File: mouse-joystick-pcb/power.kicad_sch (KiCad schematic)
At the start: 10 parts, among them J301 2.1, U301 TPSM365R6V5RDNR

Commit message: Finish routing
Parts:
- C305: LCSC C2182652 -> C6119904; Manufacturer TDK Corporation -> HRE; Manufacturer Part Number C2012X5R1A476M125AC -> CGA0805X5R476M100MT; Vendor Digi-Key -> JLCPCB; Vendor Part Number 445-8239-1-ND -> C6119904
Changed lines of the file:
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@@
   (title_block
     (title "mouse-joystick-pcb")
-    (date "2024-10-15")
+    (date "2024-10-23")
     (rev "1.0")
     (company "Peter Polidoro")
@@
       (effects (font (size 1.524 1.524)))
     )
-    (property "Vendor" "Digi-Key" (at 210.82 115.57 0)
-      (effects (font (size 1.524 1.524)) hide)
-    )
-    (property "Vendor Part Number" "445-8239-1-ND" (at 213.36 113.03 0)
+    (property "Vendor" "JLCPCB" (at 210.82 115.57 0)
+      (effects (font (size 1.524 1.524)) hide)
+    )
+    (property "Vendor Part Number" "C6119904" (at 213.36 113.03 0)
       (effects (font (size 1.524 1.524)) hide)
     )
@@
       (effects (font (size 1.27 1.27)) hide)
     )
-    (property "Manufacturer" "TDK Corporation" (at 208.28 120.65 0)
-      (effects (font (size 1.27 1.27)) hide)
-    )
-    (property "Manufacturer Part Number" "C2012X5R1A476M125AC" (at 208.28 120.65 0)
+    (property "Manufacturer" "HRE" (at 208.28 120.65 0)
+      (effects (font (size 1.27 1.27)) hide)
+    )
+    (property "Manufacturer Part Number" "CGA0805X5R476M100MT" (at 208.28 120.65 0)
       (effects (font (size 1.27 1.27)) hide)
     )
@@
       (effects (font (size 1.524 1.524)) hide)
     )
-    (property "LCSC" "C2182652" (at 208.28 120.65 0)
-      (effects (font (size 1.27 1.27)) hide)
-    )
+    (property "LCSC" "C6119904" (at 208.28 120.65 0)
+      (effects (font (size 1.27 1.27)) hide)
+    )

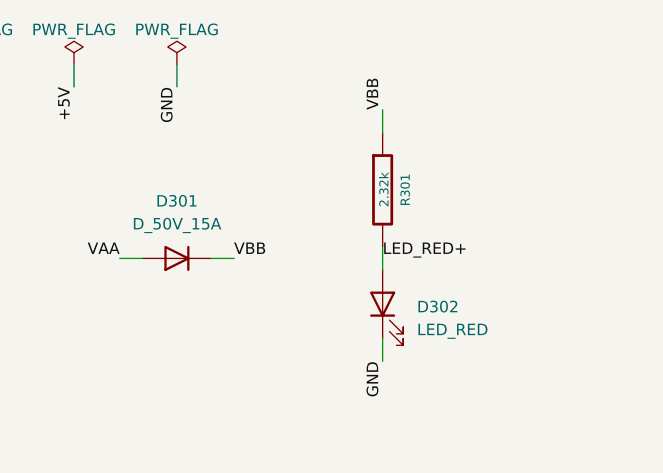
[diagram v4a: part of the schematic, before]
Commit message: Switch LED resistor to 1.5k
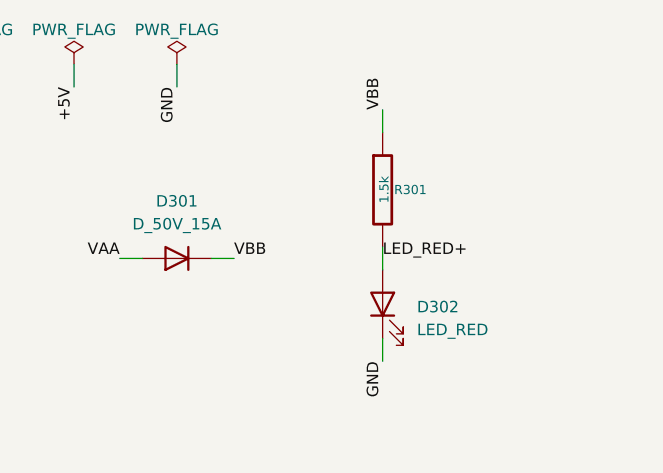
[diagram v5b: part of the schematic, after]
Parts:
- removed R301: 2.32k, Janelia:R_0805_2012Metric, symbol Janelia:R_2.32k_1W_0805
- added R301: 1.5k, Janelia:R_0805_2012Metric, symbol Janelia:R_1.5k_500mW_0805
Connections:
- net LED_RED+: now also R301.2
- net VBB: now also R301.1
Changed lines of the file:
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@@
+    )
+  )
+  (symbol (lib_id "Janelia:R_1.5k_500mW_0805") (at 187.96 59.69 0) (unit 1)
+    (in_bom yes) (on_board yes) (dnp no)
+    (property "Reference" "R301" (at 189.23 59.69 0)
+      (effects (font (size 1.016 1.016)) (justify left))
+    )
+    (property "Value" "1.5k" (at 188.1378 59.6646 90) (do_not_autoplace)
+      (effects (font (size 1.016 1.016)))
+    )
+    (property "Footprint" "Janelia:R_0805_2012Metric" (at 186.182 59.69 90)
+      (effects (font (size 0.762 0.762)) hide)
+    )
+    (property "Datasheet" "" (at 187.96 59.69 0)
+      (effects (font (size 0.762 0.762)))
+    )
+    (property "Synopsis" "RES SMD 1.5K OHM 5% 500mW" (at 197.612 52.07 90)
+      (effects (font (size 1.524 1.524)) hide)
+    )
+    (property "Package" "0805" (at 187.96 59.69 0)
+      (effects (font (size 1.524 1.524)) hide)
+    )
+    (property "Manufacturer" "PANASONIC" (at 187.96 59.69 0)
+      (effects (font (size 1.524 1.524)) hide)
+    )
+    (property "Manufacturer Part Number" "ERJP06J152V" (at 187.96 59.69 0)
+      (effects (font (size 1.524 1.524)) hide)
+    )
+    (property "Vendor" "Digi-Key" (at 187.96 59.69 0)
+      (effects (font (size 1.524 1.524)) hide)
+    )
+    (property "Vendor Part Number" "P1.5KADCT-ND" (at 187.96 59.69 0)
+      (effects (font (size 1.524 1.524)) hide)
+    )
+    (property "LCSC" "C417005" (at 187.96 59.69 0)
+      (effects (font (size 1.27 1.27)) hide)
+    )
+    (pin "2")
+    (pin "1")
+    (instances
+      (project "mouse-joystick-pcb"
+        (path "/df2b2e89-e055-4140-95de-f1df723db034/c1dd8f61-494c-402f-8e59-08309c64fc3f"
+          (reference "R301") (unit 1)
+        )
+      )
     )
   )
@@
         )
       )
-    )
-  )
-  (symbol (lib_id "Janelia:R_2.32k_1W_0805") (at 187.96 59.69 0) (unit 1)
-    (in_bom yes) (on_board yes) (dnp no)
-    (property "Reference" "R301" (at 190.5 59.69 90)
-      (effects (font (size 1.016 1.016)))
-    )
-    (property "Value" "2.32k" (at 188.1378 59.6646 90) (do_not_autoplace)
-      (effects (font (size 1.016 1.016)))
-    )
-    (property "Footprint" "Janelia:R_0805_2012Metric" (at 186.182 59.69 90)
-      (effects (font (size 0.762 0.762)) hide)
-    )
-    (property "Datasheet" "" (at 187.96 59.69 0)
-      (effects (font (size 0.762 0.762)))
-    )
-    (property "Package" "0805" (at 187.96 59.69 0)
-      (effects (font (size 1.524 1.524)) hide)
-    )
-    (property "Manufacturer" "TE Connectivity Passive Product" (at 187.96 59.69 0)
-      (effects (font (size 1.524 1.524)) hide)
-    )
-    (property "Manufacturer Part Number" "RA73F2A2K32BTD" (at 187.96 59.69 0)
-      (effects (font (size 1.524 1.524)) hide)
-    )
-    (property "Vendor" "Digi-Key" (at 187.96 59.69 0)
-      (effects (font (size 1.524 1.524)) hide)
-    )
-    (property "Vendor Part Number" "1712-RA73F2A2K32BTDCT-ND" (at 187.96 59.69 0)
-      (effects (font (size 1.524 1.524)) hide)
-    )
-    (property "Synopsis" "RA73F 2A 2K32 0.1% 5K RL" (at 197.612 52.07 90)
-      (effects (font (size 1.524 1.524)) hide)
-    )
-    (property "LCSC" "C3961061" (at 187.96 59.69 0)
-      (effects (font (size 1.27 1.27)) hide)
-    )
-    (pin "2")
-    (pin "1")
-    (instances
-      (project "mouse-joystick-pcb"
-        (path "/df2b2e89-e055-4140-95de-f1df723db034/c1dd8f61-494c-402f-8e59-08309c64fc3f"
-          (reference "R301") (unit 1)
-        )
-      )
